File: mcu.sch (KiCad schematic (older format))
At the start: 44 parts, among them J10 USB_C_Receptacle_USB2.0, J11 I2Sext_SD, J12 I2S_SD, J13 SDOUT, J14 ~CSB, J15 I2S2_MCK, J16 WCLK, J17 BCLK, J18 SCLK, J7 PD0-7, J8 PD8-15, J9 debug, SW1 SW_MEC_5E, SW2 SW_MEC_5E, U3 STM32F407VETx, Y1 8Mhz

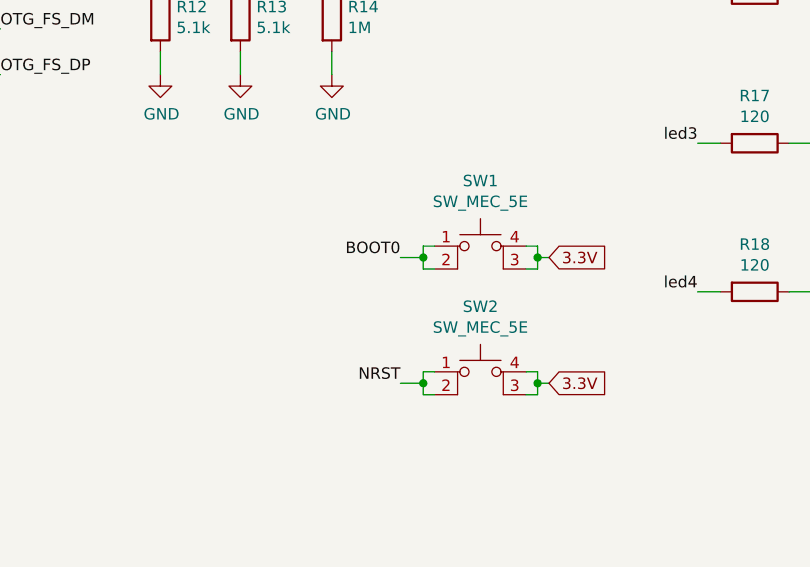
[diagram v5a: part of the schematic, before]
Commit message: Add tactile switch footprints
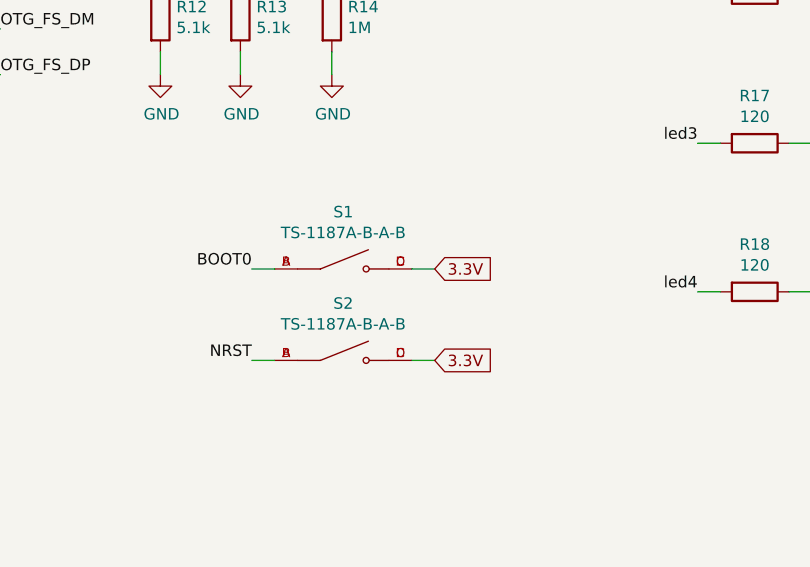
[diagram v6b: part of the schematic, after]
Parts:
- removed SW1, SW2: SW_MEC_5E, symbol Switch:SW_MEC_5E
- added S1, S2: TS-1187A-B-A-B, TactileSwitch:SW_TS-1187A-B-A-B, symbol TactileSwitch:TS-1187A-B-A-B
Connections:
- net 3.3V: now also S1.C, S1.D, S2.C, S2.D
- net BOOT0: now also S1.A, S1.B
- net NRST: now also S2.A, S2.B
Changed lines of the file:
@@
 Wire Wire Line
 	6650 4200 8200 4200
-$Comp
-L Switch:SW_MEC_5E SW1
-U 1 1 602AEEE9
-P 8850 5800
-F 0 "SW1" H 8850 6185 50  0000 C CNN
-F 1 "SW_MEC_5E" H 8850 6094 50  0000 C CNN
-F 2 "" H 8850 6100 50  0001 C CNN
-F 3 "http://www.apem.com/int/index.php?controller=attachment&id_attachment=1371" H 8850 6100 50  0001 C CNN
-	1    8850 5800
-	1    0    0    -1
-$EndComp
-$Comp
-L Switch:SW_MEC_5E SW2
-U 1 1 602B029E
-P 8850 6350
-F 0 "SW2" H 8850 6735 50  0000 C CNN
-F 1 "SW_MEC_5E" H 8850 6644 50  0000 C CNN
-F 2 "" H 8850 6650 50  0001 C CNN
-F 3 "http://www.apem.com/int/index.php?controller=attachment&id_attachment=1371" H 8850 6650 50  0001 C CNN
-	1    8850 6350
-	1    0    0    -1
-$EndComp
-Wire Wire Line
-	8650 5700 8600 5700
-Wire Wire Line
-	8600 5700 8600 5750
-Wire Wire Line
-	8600 5800 8650 5800
-Text Label 8500 5750 2    50   ~ 0
+Text Label 7850 5800 2    50   ~ 0
 BOOT0
-Wire Wire Line
-	8500 5750 8600 5750
-Connection ~ 8600 5750
-Wire Wire Line
-	8600 5750 8600 5800
-Text GLabel 9150 5750 2    50   Input ~ 0
+Text GLabel 8650 5800 2    50   Input ~ 0
 3.3V
-Wire Wire Line
-	9050 5700 9100 5700
-Wire Wire Line
-	9100 5700 9100 5750
-Wire Wire Line
-	9100 5800 9050 5800
-Wire Wire Line
-	9150 5750 9100 5750
-Connection ~ 9100 5750
-Wire Wire Line
-	9100 5750 9100 5800
-Text Label 8500 6300 2    50   ~ 0
+Text Label 7850 6200 2    50   ~ 0
 NRST
-Wire Wire Line
-	8500 6300 8600 6300
-Wire Wire Line
-	8600 6300 8600 6250
-Wire Wire Line
-	8600 6250 8650 6250
-Wire Wire Line
-	8600 6300 8600 6350
-Wire Wire Line
-	8600 6350 8650 6350
-Connection ~ 8600 6300
-Text GLabel 9150 6300 2    50   Input ~ 0
+Text GLabel 8650 6200 2    50   Input ~ 0
 3.3V
-Wire Wire Line
-	9050 6250 9100 6250
-Wire Wire Line
-	9100 6250 9100 6300
-Wire Wire Line
-	9100 6350 9050 6350
-Wire Wire Line
-	9150 6300 9100 6300
-Connection ~ 9100 6300
-Wire Wire Line
-	9100 6300 9100 6350
 Wire Wire Line
 	3750 6950 4400 6950
@@
 NoConn ~ 3800 6000
 NoConn ~ 3800 6100
+$Comp
+L TactileSwitch:TS-1187A-B-A-B S1
+U 1 1 60C1533E
+P 8250 5800
+F 0 "S1" H 8250 6049 50  0000 C CNN
+F 1 "TS-1187A-B-A-B" H 8250 5958 50  0000 C CNN
+F 2 "TactileSwitch:SW_TS-1187A-B-A-B" H 8250 5800 50  0001 L BNN
+F 3 "" H 8250 5800 50  0001 L BNN
+F 4 "XKB Industrial Precision" H 8250 5800 50  0001 L BNN "MANUFACTURER"
+F 5 "Manufacturer Recommendations" H 8250 5800 50  0001 L BNN "STANDARD"
+F 6 "1.5mm" H 8250 5800 50  0001 L BNN "MAXIMUM_PACKAGE_HEIGHT"
+F 7 "A0" H 8250 5800 50  0001 L BNN "PARTREV"
+	1    8250 5800
+	1    0    0    -1
+$EndComp
+$Comp
+L TactileSwitch:TS-1187A-B-A-B S2
+U 1 1 60C15961
+P 8250 6200
+F 0 "S2" H 8250 6449 50  0000 C CNN
+F 1 "TS-1187A-B-A-B" H 8250 6358 50  0000 C CNN
+F 2 "TactileSwitch:SW_TS-1187A-B-A-B" H 8250 6200 50  0001 L BNN
+F 3 "" H 8250 6200 50  0001 L BNN
+F 4 "XKB Industrial Precision" H 8250 6200 50  0001 L BNN "MANUFACTURER"
+F 5 "Manufacturer Recommendations" H 8250 6200 50  0001 L BNN "STANDARD"
+F 6 "1.5mm" H 8250 6200 50  0001 L BNN "MAXIMUM_PACKAGE_HEIGHT"
+F 7 "A0" H 8250 6200 50  0001 L BNN "PARTREV"
+	1    8250 6200
+	1    0    0    -1
+$EndComp
+Wire Wire Line
+	7850 5800 7950 5800
+Wire Wire Line
+	7850 6200 7950 6200
+Wire Wire Line
+	8650 6200 8550 6200
+Wire Wire Line
+	8550 5800 8650 5800
 $EndSCHEMATC
